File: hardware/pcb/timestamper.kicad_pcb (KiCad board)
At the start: 2 copper layers, 75 x 100 mm, 111 parts, among them J1 Conn_Coaxial, J2 Conn_Coaxial, J3 Conn_Coaxial, J4 JTAG, J5 ISP, J6 Conn_Coaxial, J7 USB_B_Micro, U1 AP1117-33, U10 ATMEGA328-AU, U11 74HC04, U2 TLV71318PDBV, U3 CDCE925, U4 USBLC6-2SC6, U5 74AHC1G14, U6 74AHC1G14, U7 LMV7219?, U8 CH340G, U9 XC9572XL-VQ44, Y1 12MHz, Y2 8MHz

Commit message: Forgot to change L1 footprint
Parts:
- L1: footprint Resistors_SMD:R_0603 -> Inductor_SMD:L_0603_1608Metric
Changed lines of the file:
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@@
     )
   )
-  (module Resistors_SMD:R_0603 (layer F.Cu)
-    (at 73.4 100.1 270)
-    (descr "Resistor SMD 0603, reflow soldering, Vishay (see dcrcw.pdf)")
-    (tags "resistor 0603")
-    (attr smd)
-    (fp_text reference L1 (at -0.1 1.6 270) (layer F.SilkS)
-      (effects (font (size 1 1) (thickness 0.15)))
-    )
-    (fp_text value L (at 0 1.5 270) (layer F.Fab)
-      (effects (font (size 1 1) (thickness 0.15)))
-    )
-    (fp_text user %R (at 0 0 270) (layer F.Fab)
-      (effects (font (size 0.4 0.4) (thickness 0.075)))
-    )
-    (fp_line (start -0.8 0.4) (end -0.8 -0.4) (layer F.Fab) (width 0.1))
-    (fp_line (start 0.8 0.4) (end -0.8 0.4) (layer F.Fab) (width 0.1))
-    (fp_line (start 0.8 -0.4) (end 0.8 0.4) (layer F.Fab) (width 0.1))
-    (fp_line (start -0.8 -0.4) (end 0.8 -0.4) (layer F.Fab) (width 0.1))
-    (fp_line (start 0.5 0.68) (end -0.5 0.68) (layer F.SilkS) (width 0.12))
-    (fp_line (start -0.5 -0.68) (end 0.5 -0.68) (layer F.SilkS) (width 0.12))
-    (fp_line (start -1.25 -0.7) (end 1.25 -0.7) (layer F.CrtYd) (width 0.05))
-    (fp_line (start -1.25 -0.7) (end -1.25 0.7) (layer F.CrtYd) (width 0.05))
-    (fp_line (start 1.25 0.7) (end 1.25 -0.7) (layer F.CrtYd) (width 0.05))
-    (fp_line (start 1.25 0.7) (end -1.25 0.7) (layer F.CrtYd) (width 0.05))
-    (pad 1 smd rect (at -0.75 0 270) (size 0.5 0.9) (layers F.Cu F.Paste F.Mask)
-      (net 7 +1V8))
-    (pad 2 smd rect (at 0.75 0 270) (size 0.5 0.9) (layers F.Cu F.Paste F.Mask)
-      (net 3 "Net-(C5-Pad1)"))
-    (model ${KISYS3DMOD}/Resistors_SMD.3dshapes/R_0603.wrl
-      (at (xyz 0 0 0))
-      (scale (xyz 1 1 1))
-      (rotate (xyz 0 0 0))
-    )
-  )
   (module Capacitor_SMD:C_0603_1608Metric (layer F.Cu)
     (at 83.2 137.8 180)
@@
       (at (xyz 0 0 0))
       (scale (xyz 1 1 1))
+      (rotate (xyz 0 0 0))
+    )
+  )
+  (module Inductor_SMD:L_0603_1608Metric (layer F.Cu)
+    (at 73.4 100.1 270)
+    (descr "Inductor SMD 0603 (1608 Metric), square (rectangular) end terminal, IPC_7351 nominal, (Body size source: http://www.tortai-tech.com/upload/download/2011102023233369053.pdf), generated with kicad-footprint-generator")
+    (tags inductor)
+    (attr smd)
+    (fp_text reference L1 (at 0 -1.43 270) (layer F.SilkS)
+      (effects (font (size 1 1) (thickness 0.15)))
+    )
+    (fp_text value L (at 0 1.43 270) (layer F.Fab)
+      (effects (font (size 1 1) (thickness 0.15)))
+    )
+    (fp_line (start -0.8 0.4) (end -0.8 -0.4) (layer F.Fab) (width 0.1))
+    (fp_line (start -0.8 -0.4) (end 0.8 -0.4) (layer F.Fab) (width 0.1))
+    (fp_line (start 0.8 -0.4) (end 0.8 0.4) (layer F.Fab) (width 0.1))
+    (fp_line (start 0.8 0.4) (end -0.8 0.4) (layer F.Fab) (width 0.1))
+    (fp_line (start -0.162779 -0.51) (end 0.162779 -0.51) (layer F.SilkS) (width 0.12))
+    (fp_line (start -0.162779 0.51) (end 0.162779 0.51) (layer F.SilkS) (width 0.12))
+    (fp_line (start -1.48 0.73) (end -1.48 -0.73) (layer F.CrtYd) (width 0.05))
+    (fp_line (start -1.48 -0.73) (end 1.48 -0.73) (layer F.CrtYd) (width 0.05))
+    (fp_line (start 1.48 -0.73) (end 1.48 0.73) (layer F.CrtYd) (width 0.05))
+    (fp_line (start 1.48 0.73) (end -1.48 0.73) (layer F.CrtYd) (width 0.05))
+    (fp_text user %R (at 0 0 270) (layer F.Fab)
+      (effects (font (size 0.4 0.4) (thickness 0.06)))
+    )
+    (pad 1 smd roundrect (at -0.7875 0 270) (size 0.875 0.95) (layers F.Cu F.Paste F.Mask) (roundrect_rratio 0.25)
+      (net 7 +1V8))
+    (pad 2 smd roundrect (at 0.7875 0 270) (size 0.875 0.95) (layers F.Cu F.Paste F.Mask) (roundrect_rratio 0.25)
+      (net 3 "Net-(C5-Pad1)"))
+    (model ${KISYS3DMOD}/Inductor_SMD.3dshapes/L_0603_1608Metric.wrl
+      (at (xyz 0 0 0))
+      (scale (xyz 1 1 1))

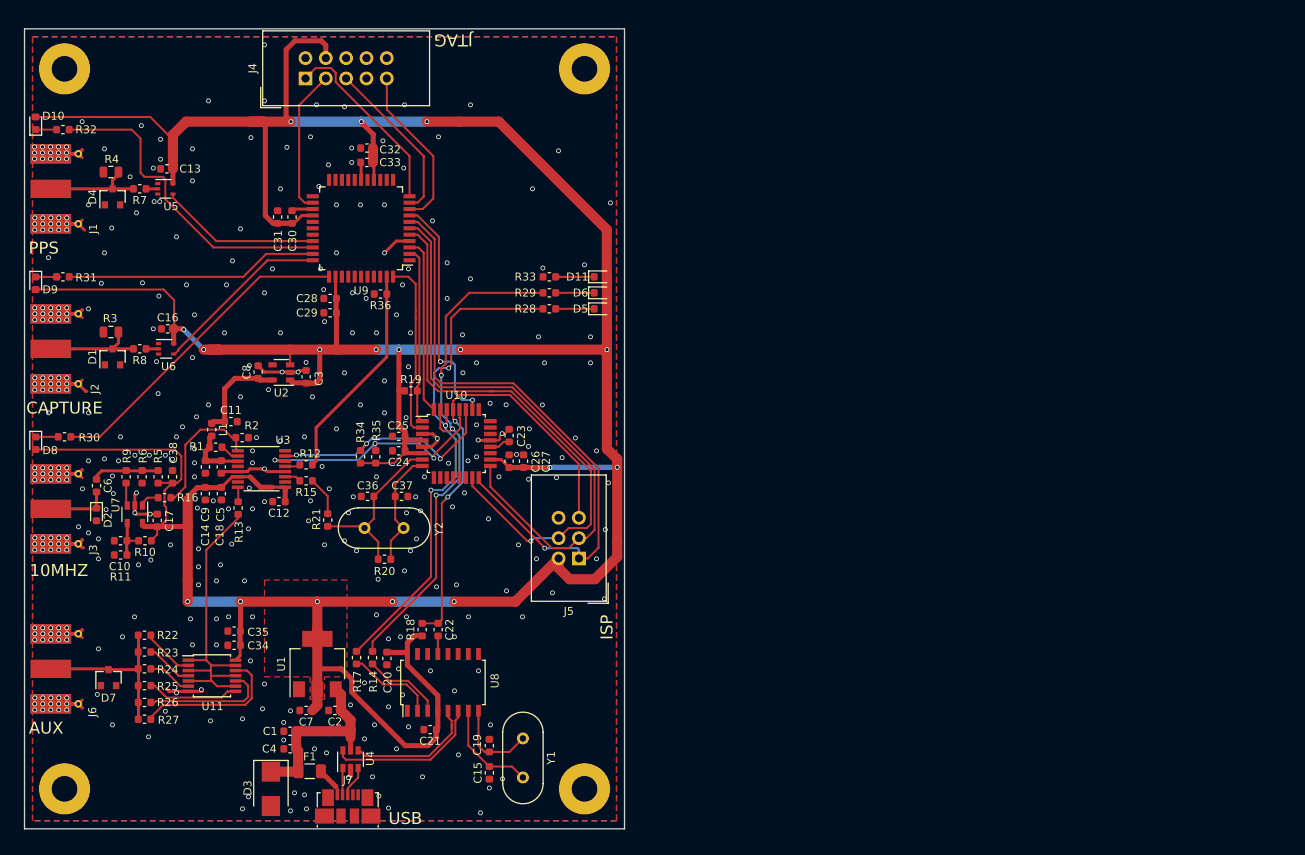
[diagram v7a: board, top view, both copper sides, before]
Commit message: Added SMA 3d model
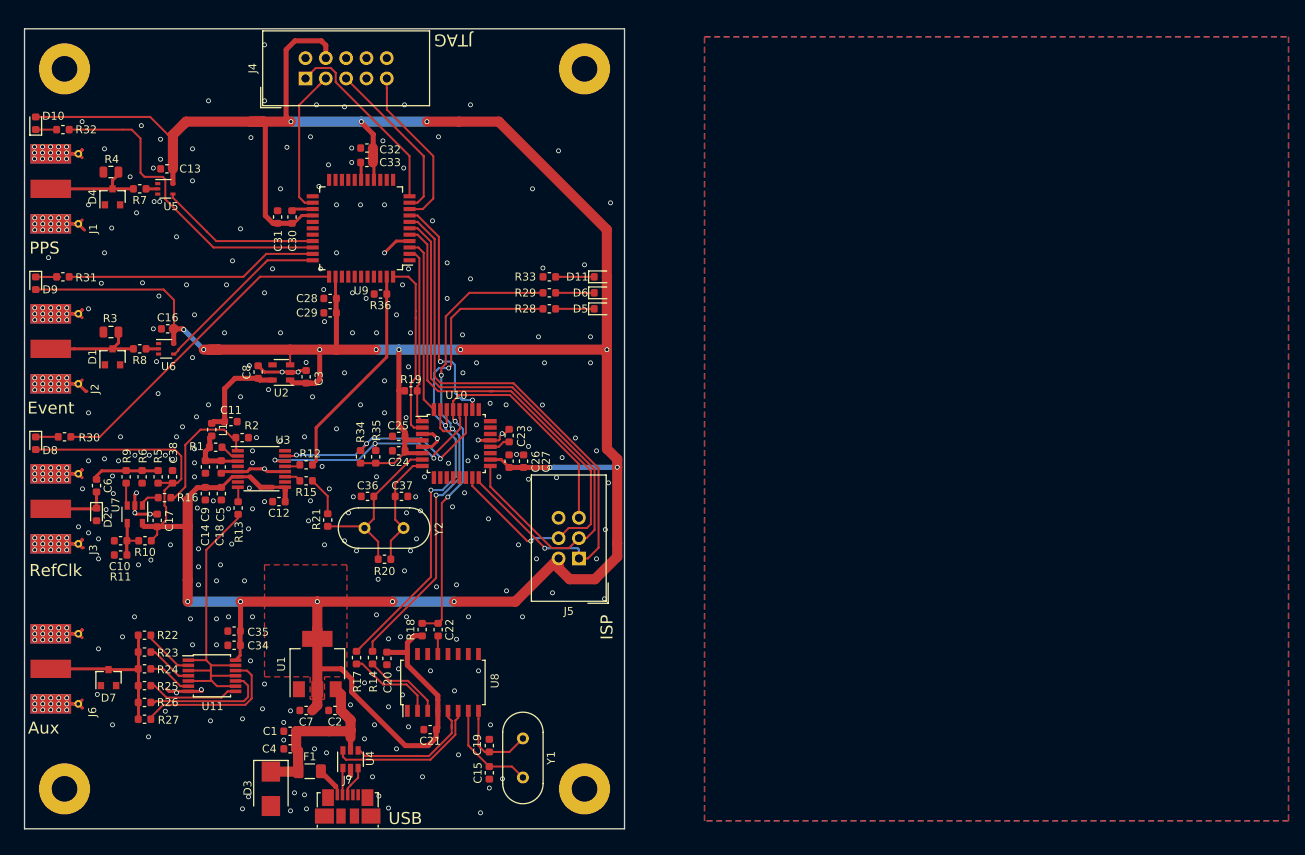
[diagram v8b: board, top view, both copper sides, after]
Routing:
- net GND: vias 379 -> 378
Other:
- board text added: "Aux"
- board text added: "Event"
- board text added: "RefClk"
- board text removed: "10MHZ"
- board text removed: "AUX"
- board text removed: "CAPTURE"
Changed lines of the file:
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@@
     (thickness 1.6)
     (drawings 11)
-    (tracks 1119)
+    (tracks 1118)
     (zones 0)
     (modules 111)
@@
   )
   (setup
-    (last_trace_width 0.381)
+    (last_trace_width 0.635)
     (user_trace_width 0.254)
     (user_trace_width 0.381)
@@
       (rotate (xyz 0 0 0))
     )
+    (model ${KIPRJMOD}/3dmodels/SMA_Board_Edge_Molex_732511150.step
+      (offset (xyz -4 0 0))
+      (scale (xyz 1 1 1))
+      (rotate (xyz 0 0 90))
+    )
   )
   (module Connectors_Molex:Molex_SMA_Jack_Edge_Mount (layer F.Cu)
@@
       (rotate (xyz 0 0 0))
     )
+    (model ${KIPRJMOD}/3dmodels/SMA_Board_Edge_Molex_732511150.step
+      (offset (xyz -4 0 0))
+      (scale (xyz 1 1 1))
+      (rotate (xyz 0 0 90))
+    )
   )
   (module Connectors_Molex:Molex_SMA_Jack_Edge_Mount (layer F.Cu)
@@
       (rotate (xyz 0 0 0))
     )
+    (model ${KIPRJMOD}/3dmodels/SMA_Board_Edge_Molex_732511150.step
+      (offset (xyz -4 0 0))
+      (scale (xyz 1 1 1))
+      (rotate (xyz 0 0 90))
+    )
   )
   (module Connectors_Molex:Molex_SMA_Jack_Edge_Mount (layer F.Cu)
@@
       (rotate (xyz 0 0 0))
     )
+    (model ${KIPRJMOD}/3dmodels/SMA_Board_Edge_Molex_732511150.step
+      (offset (xyz -4 0 0))
+      (scale (xyz 1 1 1))
+      (rotate (xyz 0 0 90))
+    )
   )
   (module Capacitor_SMD:C_0603_1608Metric (layer F.Cu)
@@
     (effects (font (size 1.5 1.5) (thickness 0.3)))
   )
-  (gr_text 10MHZ (at 54.3 117.7) (layer F.SilkS)
+  (gr_text RefClk (at 53.9 117.7) (layer F.SilkS)
     (effects (font (size 1.5 1.5) (thickness 0.3)))
   )
@@
     (effects (font (size 1.5 1.5) (thickness 0.3)))
   )
-  (gr_text CAPTURE (at 55 97.4) (layer F.SilkS)
+  (gr_text Event (at 53.3 97.4) (layer F.SilkS)
     (effects (font (size 1.5 1.5) (thickness 0.3)))
   )
-  (gr_text PPS (at 52.4 77.4) (layer F.SilkS)
+  (gr_text PPS (at 52.5 77.4) (layer F.SilkS)
     (effects (font (size 1.5 1.5) (thickness 0.3)))
   )
-  (gr_text AUX (at 52.7 137.4) (layer F.SilkS)
+  (gr_text Aux (at 52.4 137.4) (layer F.SilkS)
     (effects (font (size 1.5 1.5) (thickness 0.3)))
   )
@@
   (via (at 66.1 87.5) (size 0.6) (drill 0.4) (layers F.Cu B.Cu) (net 1))
   (via (at 66.5 91.6) (size 0.6) (drill 0.4) (layers F.Cu B.Cu) (net 1))
-  (via (at 53 98) (size 0.6) (drill 0.4) (layers F.Cu B.Cu) (net 1))
   (via (at 58 98) (size 0.6) (drill 0.4) (layers F.Cu B.Cu) (net 1))
   (via (at 62 101) (size 0.6) (drill 0.4) (layers F.Cu B.Cu) (net 1))
@@
   (via (at 108.25 137) (size 0.6) (drill 0.4) (layers F.Cu B.Cu) (net 1))
   (via (at 106.75 130.25) (size 0.6) (drill 0.4) (layers F.Cu B.Cu) (net 1))
-  (via (at 103.75 126) (size 0.6) (drill 0.4) (layers F.Cu B.Cu) (net 1))
+  (via (at 104 126.3) (size 0.6) (drill 0.4) (layers F.Cu B.Cu) (net 1))
   (via (at 105.5 123.5) (size 0.6) (drill 0.4) (layers F.Cu B.Cu) (net 1))
   (via (at 116 120.5) (size 0.6) (drill 0.4) (layers F.Cu B.Cu) (net 1))
@@
     (polygon
       (pts
-        (xy 51 51) (xy 124 51) (xy 124 149) (xy 51 149)
+        (xy 135 51) (xy 208 51) (xy 208 149) (xy 135 149)
       )
     )
@@
     (polygon
       (pts
-        (xy 51 51) (xy 124 51) (xy 124 149) (xy 51 149)
+        (xy 135 51) (xy 208 51) (xy 208 149) (xy 135 149)
       )
     )
@@
       (pts
         (xy 80 131) (xy 85.7 131) (xy 85.7 133.8) (xy 87.5 133.8) (xy 87.5 131)
-        (xy 90.3 131) (xy 90.3 118.9) (xy 80 118.9)
+        (xy 90.3 131) (xy 90.3 117) (xy 80 117)
       )
     )
